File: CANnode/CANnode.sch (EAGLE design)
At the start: 244 parts, among them IC1 ISO1050DUB, IC2 ISO1050DUB, Q1 FDV302P, Q3 FDV302P, U1 LM324PW, U10 FT2232HL, U11 93LC56C-I/SN, U2 TPS70445_PWP_24, U3 LM324PW, U4 LM324PW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

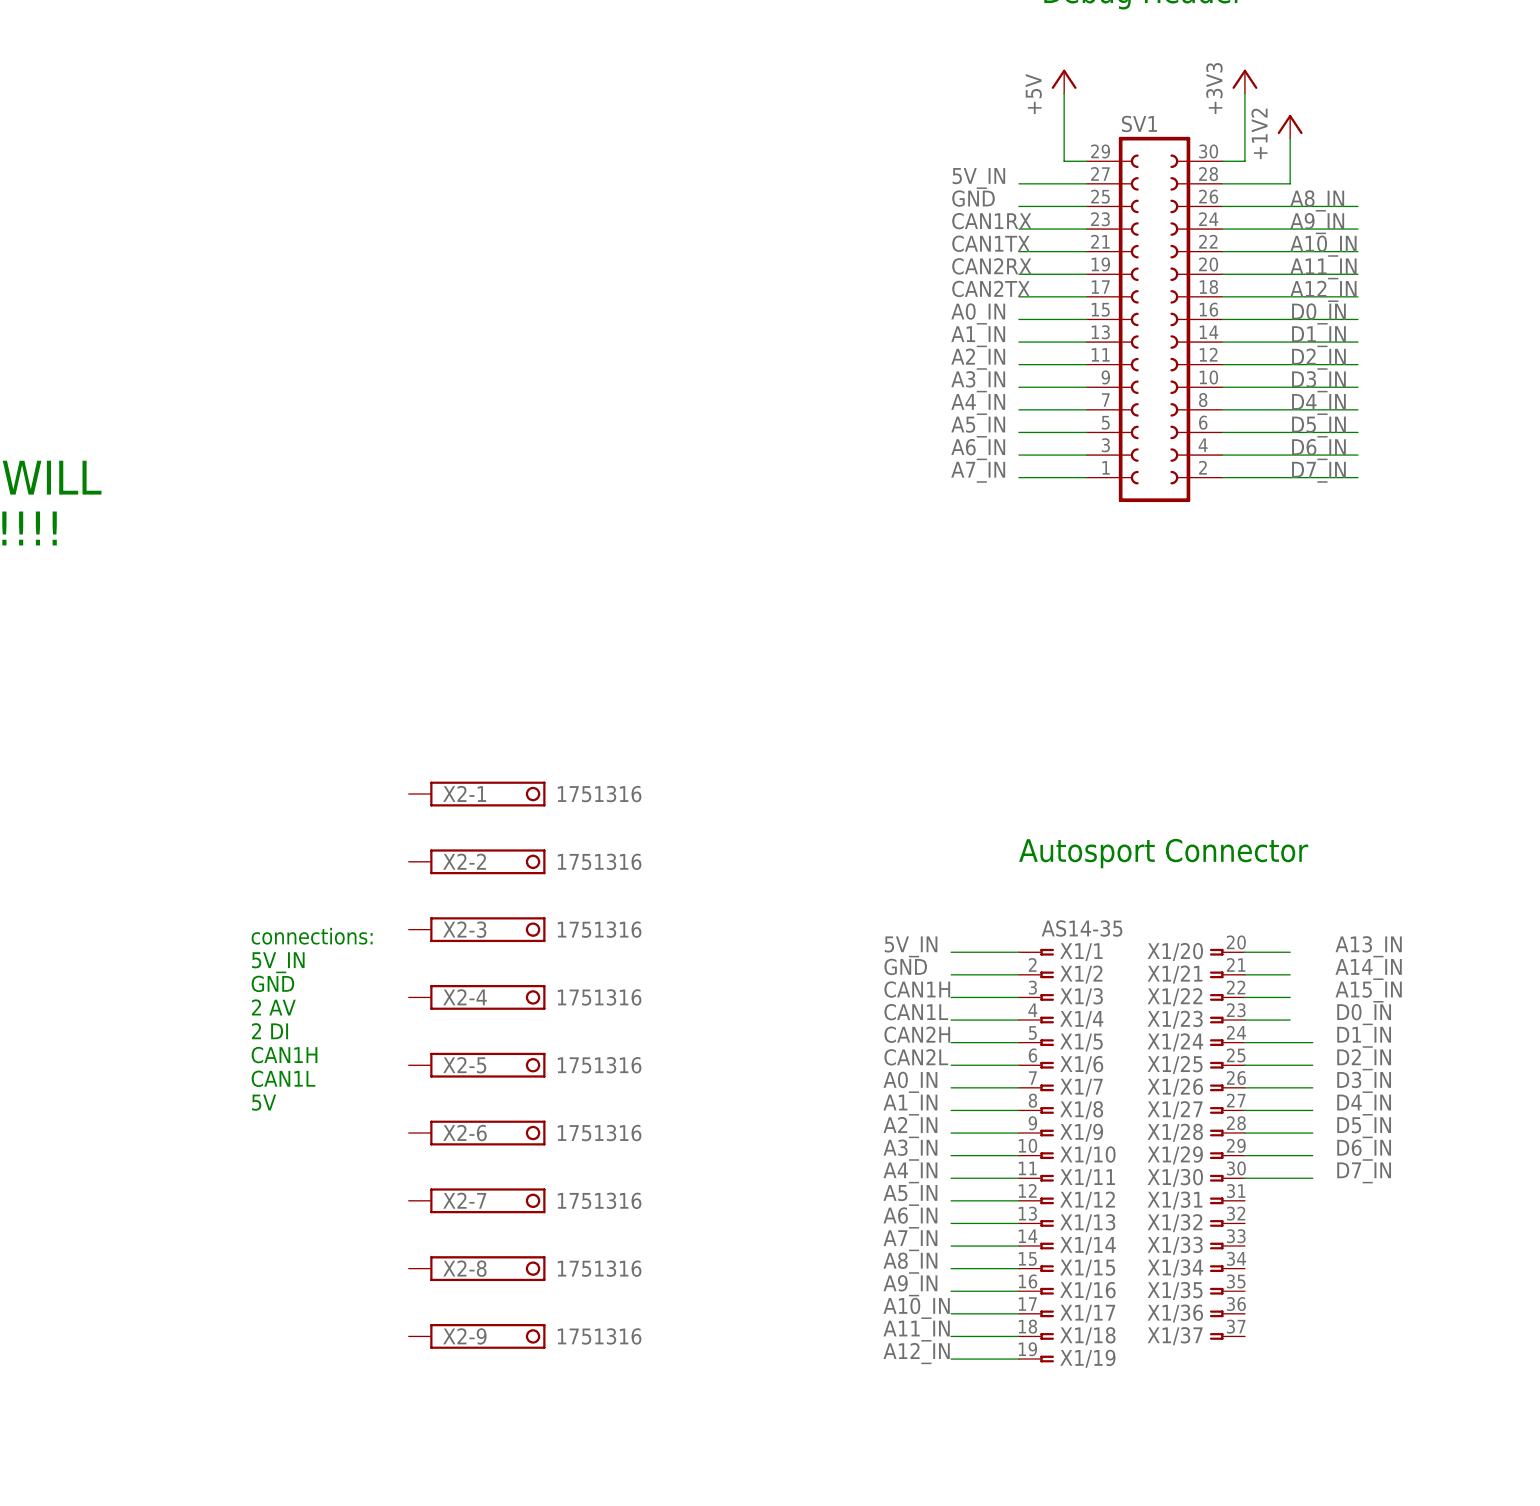
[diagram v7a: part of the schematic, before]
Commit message: Started routing Debug headers
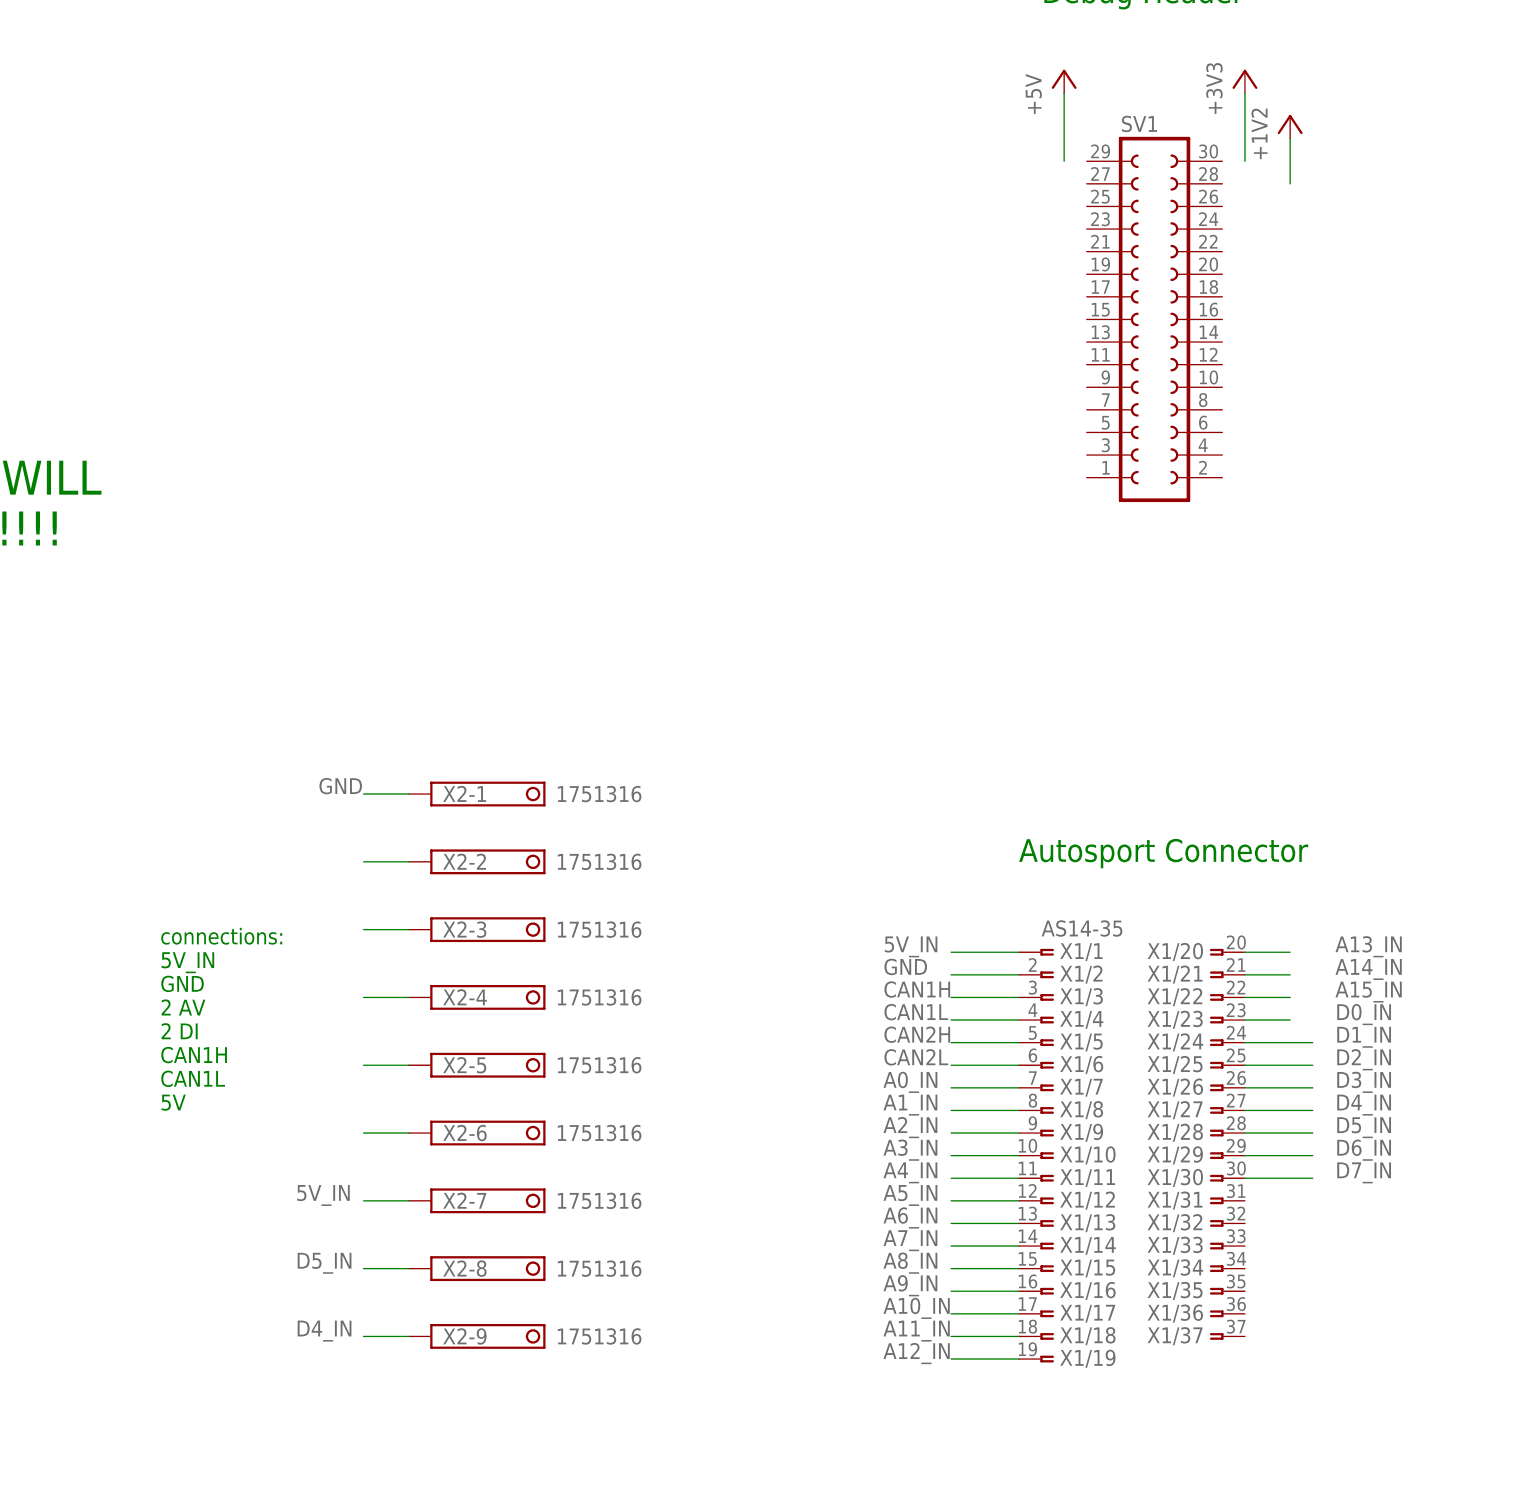
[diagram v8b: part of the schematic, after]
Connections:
- new net N$44: X2-6.K
- new net N$69: X2-5.K
- new net N$70: X2-4.K
- new net N$71: X2-3.K
- new net N$72: X2-2.K
- net +1V2: no longer SV1.28
- net +3V3: no longer SV1.30
- net +5V: no longer SV1.29
- net 5V_IN: now also X2-7.K; no longer SV1.27
- net A0_IN: no longer SV1.15
- net A10_IN: no longer SV1.22
- net A11_IN: no longer SV1.20
- net A12_IN: no longer SV1.18
- net A1_IN: no longer SV1.13
- net A2_IN: no longer SV1.11
- net A3_IN: no longer SV1.9
- net A4_IN: no longer SV1.7
- net A5_IN: no longer SV1.5
- net A6_IN: no longer SV1.3
- net A7_IN: no longer SV1.1
- net A8_IN: no longer SV1.26
- net A9_IN: no longer SV1.24
- net CAN1RX: no longer SV1.23
- net CAN1TX: no longer SV1.21
- net CAN2RX: no longer SV1.19
- net CAN2TX: no longer SV1.17
- net D0_IN: no longer SV1.16
- net D1_IN: no longer SV1.14
- net D2_IN: no longer SV1.12
- net D3_IN: no longer SV1.10
- net D4_IN: now also X2-9.K; no longer SV1.8
- net D5_IN: now also X2-8.K; no longer SV1.6
- net D6_IN: no longer SV1.4
- net D7_IN: no longer SV1.2
- net GND: now also X2-1.K; no longer SV1.25
